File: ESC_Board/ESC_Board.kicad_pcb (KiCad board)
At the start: 4 copper layers, 73.2 x 50.8 mm, 199 parts, among them J1 63824-1, J2 63824-1, J3 63824-1, Q1 AO3400A, Q10 SIR182DP, Q11 SIR182Dp, Q12 SIR182DP, Q13 SIR182DP, Q14 SIR182DP, Q15 AO3400A, Q16 SIR182DP, Q17 SIR182DP, Q18 SIR182Dp, Q19 SIR182DP, Q2 AO3400A, Q20 SIR182DP, Q21 SIR182DP, Q22 AO3400A, Q23 SIR182DP, Q24 SIR182DP, Q25 SIR182Dp, Q26 SIR182DP, Q27 SIR182DP, Q28 SIR182DP, Q3 SIR182DP, Q4 SIR182DP, Q5 SIR182DP, Q6 SIR182Dp, Q7 SIR182DP, Q8 SIR182DP, Q9 SIR182DP, U10 DRV8300DRGER, U11 STM32F051K8Ux, U12 INA180A1, U13 DRV8300DRGER, U14 STM32F051K8Ux, U15 INA180A1, U2 STM32F051K8Ux, U3 INA180A1, U4 TPS62153RGTT, U5 DRV8300DRGER, U6 TLV76601QWDRBRQ1, U7 STM32F051K8Ux, U8 DRV8300DRGER, U9 INA180A1

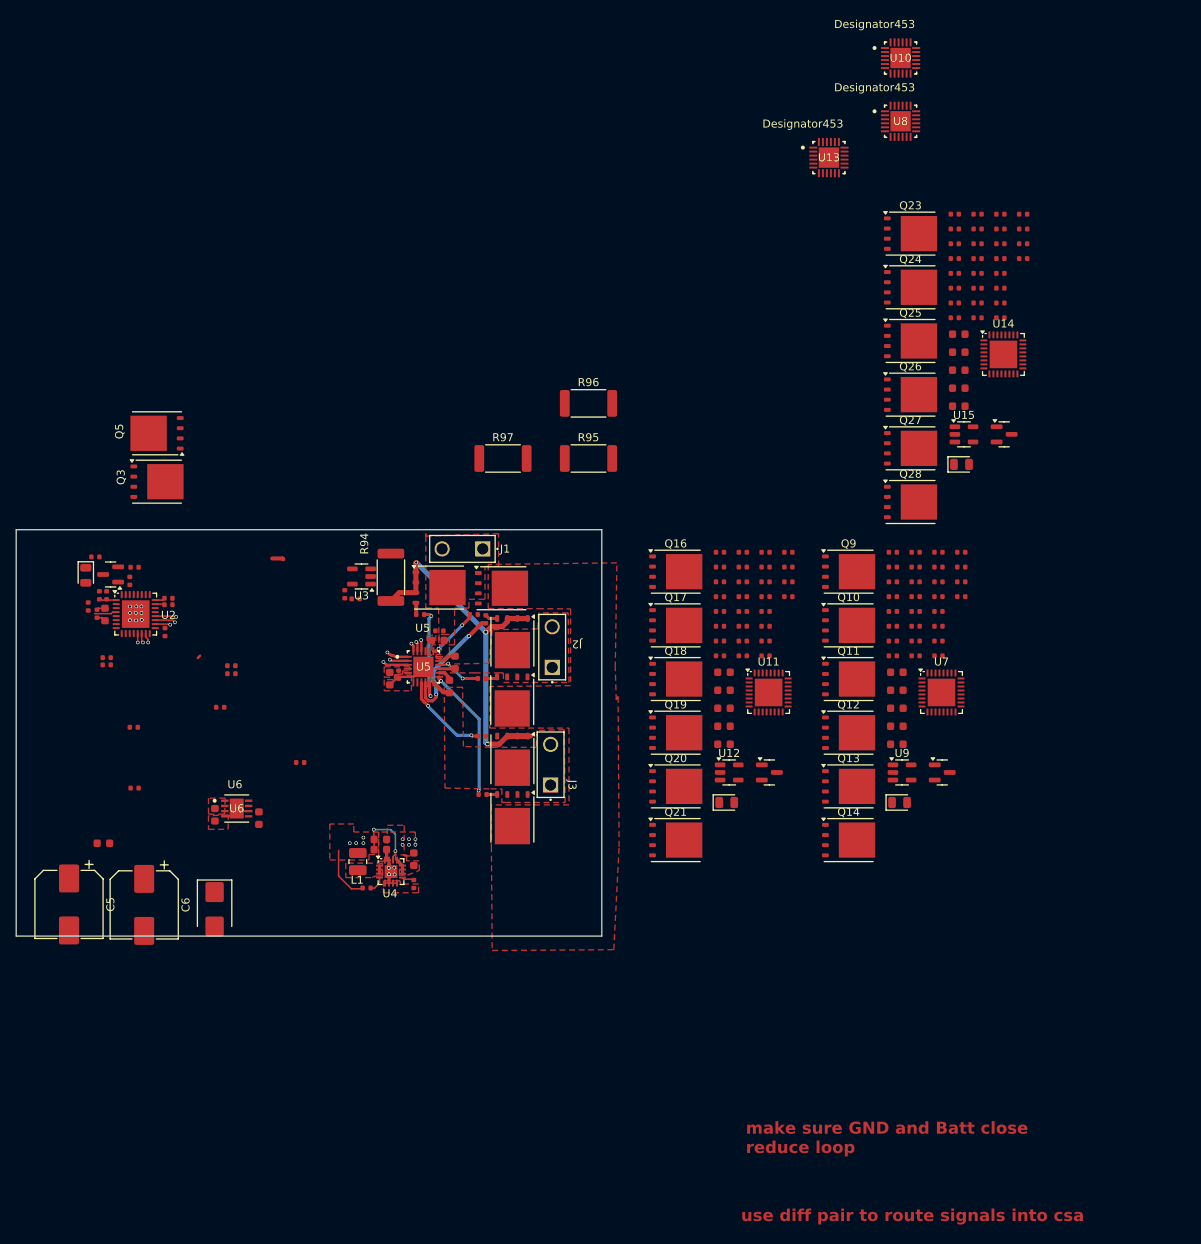
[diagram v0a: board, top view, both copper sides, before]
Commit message: ESC Board: Major overhauls to schematic, preliminary layout
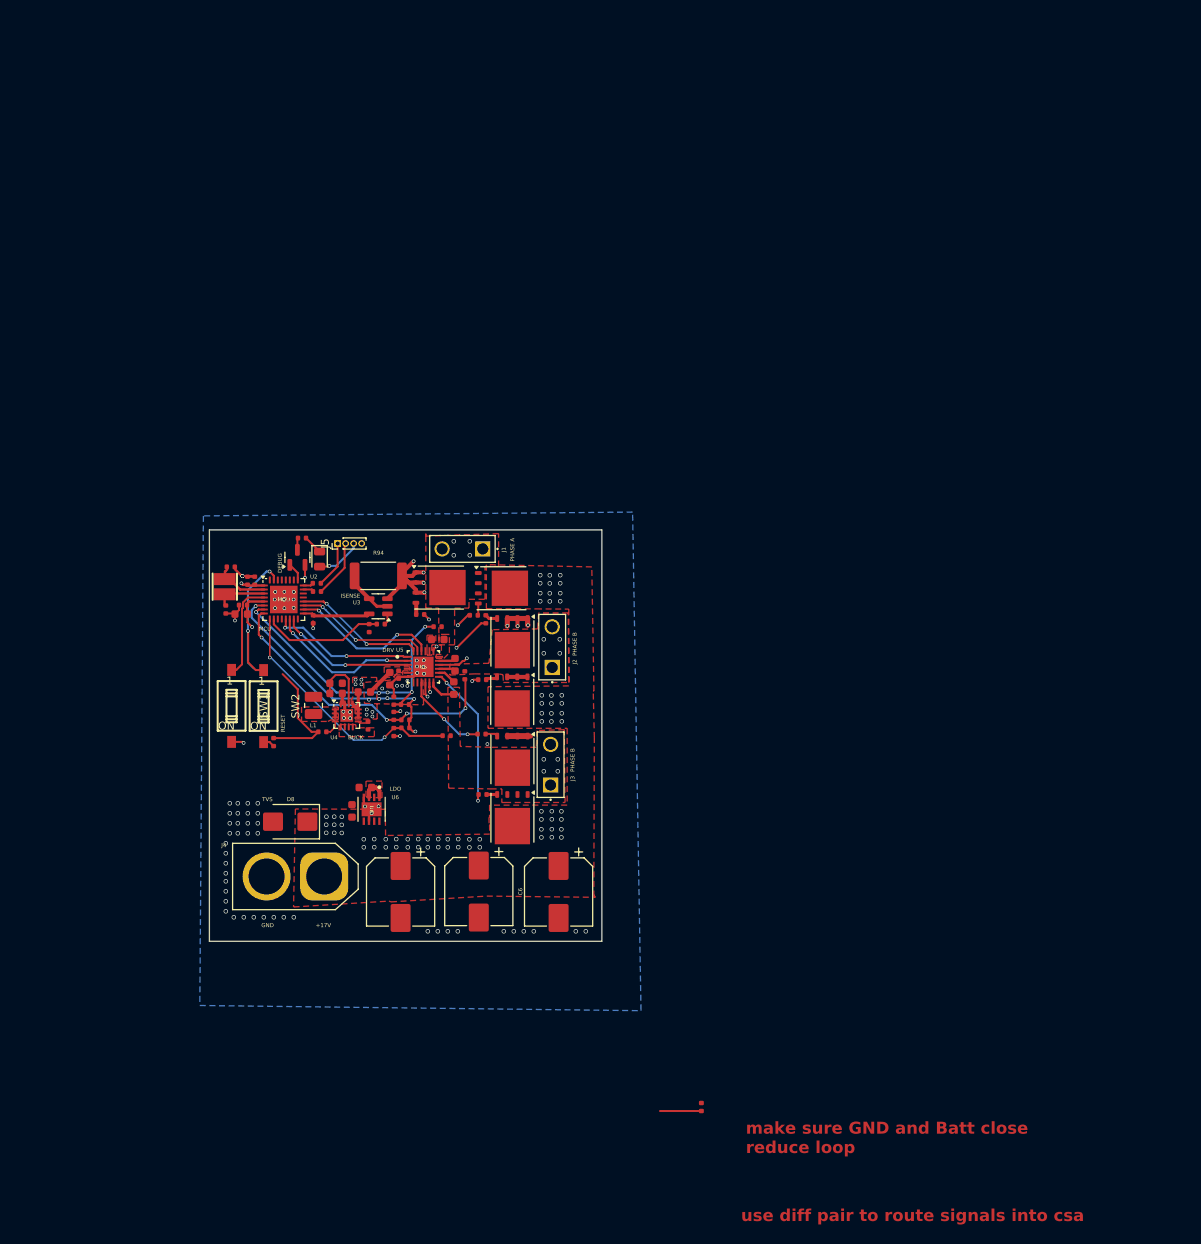
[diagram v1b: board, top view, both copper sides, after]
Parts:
- removed C14, C17, C2, C22, C3, C32, C34, C35, C4, C42, C44, C45: 100nF, PCM_JLCPCB:C_0402
- removed C18, C36, C46: 4.7uF, PCM_JLCPCB:C_0402
- removed C19, C40, C50: 10nF, PCM_JLCPCB:C_0402
- removed C27, C29, C30, C31, C37, C38, C39, C41, C47, C48, C49, C51: 1uF, PCM_JLCPCB:C_0603
- removed C28, C33, C43: 10uF, PCM_JLCPCB:C_0603
- removed D2, D4, D5: Red, PCM_JLCPCB:D_0805
- removed Q10, Q12, Q13, Q14, Q16, Q17, Q19, Q20, Q21, Q23, Q24, Q26, Q27, Q28, Q9: SIR182DP, Package_TO_SOT_SMD:TDSON-8-1
- removed Q11, Q18, Q25: SIR182Dp, Package_TO_SOT_SMD:TDSON-8-1
- removed Q15, Q2, Q22: AO3400A, PCM_JLCPCB:Q_SOT-23
- removed the Q3 at (58.4, 86.3)
- removed the Q5 at (58.4, 80.2)
- removed R10, R12, R28, R29, R30, R35, R37, R40, R42, R43, R47, R48, R49, R50, R56, R58, R62, R64, R66, R70, R71, R72, R73, R79, R81, R85, R87, R89, R93: 10kΩ, PCM_JLCPCB:R_0402
- removed R31, R32, R33, R34, R38, R39, R45, R46, R52, R53, R54, R55, R60, R61, R68, R69, R75, R76, R78, R8, R83, R84, R9, R91, R92: 22Ω, PCM_JLCPCB:R_0402
- removed R36, R41, R44, R57, R6, R63, R65, R67, R80, R86, R88, R90: 1kΩ, PCM_JLCPCB:R_0402
- removed R4, R51, R74: 75Ω, PCM_JLCPCB:R_0402
- removed R95, R96, R97: 3.0m, Resistor_SMD:R_2512_6332Metric
- removed U10, U13, U8: DRV8300DRGER, DRV:RGE0024B-IPC_A
- removed U11, U14, U7: STM32F051K8Ux, Package_DFN_QFN:QFN-32-1EP_5x5mm_P0.5mm_EP3.45x3.45mm
- removed U12, U15, U9: INA180A1, Package_TO_SOT_SMD:SOT-23-5
- added C55: 22pF, PCM_JLCPCB:C_0402, F.Cu at (67.6, 97.0)
- added C8: 100uF, Capacitor_SMD:CP_Elec_8x10, F.Cu at (108.6, 137.6)
- added J4: Conn_01x02_Pin, Connector_AMASS:AMASS_XT60-F_1x02_P7.20mm_Vertical, F.Cu at (79.3, 135.7)
- added J5: Conn_01x04_Pin, Connector_PinHeader_1.00mm:PinHeader_1x04_P1.00mm_Vertical, F.Cu at (81.0, 94.0)
- added R1: 100Ω, PCM_JLCPCB:R_0402, F.Cu at (78.4, 100.0)
- added R5: 100Ω, PCM_JLCPCB:R_0402, F.Cu at (78.4, 99.0)
- added SW1: SW_SPST, easy:SW-SMD_2P-L3.5-W6.2-P2.54-LS9.8, F.Cu at (67.7, 114.3)
- added SW2: SW_SPST, easy:SW-SMD_2P-L3.5-W6.2-P2.54-LS9.8, F.Cu at (71.7, 114.3)
- added Y1: Crystal_Small, easy:OSC-SMD_2P-L3.2-W2.5, F.Cu at (66.9, 99.4)
- C52: value 1uF -> 22pF; footprint PCM_JLCPCB:C_0603 -> PCM_JLCPCB:C_0402
- moved R77 109.8 mm to (126.5, 164.5), turned to 90 degrees
- moved C6 41.9 mm to (98.6, 137.5)
- moved C5 41.5 mm to (88.9, 137.6)
- moved R27 39.5 mm to (94.6, 118.0)
- moved R22 38.1 mm to (89.5, 116.1), turned to 180 degrees
- moved R23 36.4 mm to (88.0, 115.6), turned to 90 degrees
- moved C52 33.0 mm to (67.0, 102.3), turned to -90 degrees
- moved R26 32.5 mm to (88.0, 117.6), turned to -90 degrees
- moved D1 29.3 mm to (78.7, 96.0)
- moved R11 27.9 mm to (73.0, 118.8), turned to -90 degrees
- moved R3 25.9 mm to (76.5, 93.3), turned to 0 degrees
- moved Q1 23.4 mm to (76.0, 95.8), turned to 90 degrees
- moved R25 23.3 mm to (89.5, 117.1), turned to 180 degrees
- moved R24 23.3 mm to (96.9, 110.5), turned to 90 degrees
- moved R14 22.0 mm to (89.4, 114.2), turned to 180 degrees
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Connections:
- C52 pad 1: +17V -> Net-(U2-PF1)
- D8 pad 2: -LiPo -> GND
- R11 pad 1: GND -> +3.3V
- U2 pad 2: unconnected-(U2-PF0-Pad2) -> Net-(U2-PF0)
- U2 pad 25: unconnected-(U2-PA15-Pad25) -> Net-(Q1-G)
- U2 pad 3: unconnected-(U2-PF1-Pad3) -> Net-(U2-PF1)
- U2 pad 32: Net-(Q1-G) -> unconnected-(U2-PB8-Pad32)
- U2 pad 4: /SWDR -> Net-(SW1-A)
- U4 pad 6: AGND -> GND
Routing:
- net /BEMFB: track 0.00 -> 37.8 mm, vias 0 -> 4
- net /BEMFA: track 0.00 -> 37.8 mm, vias 0 -> 3
- net /BEMFCOMMON: track 0.00 -> 32.5 mm, vias 0 -> 3
- net /BEMFC: track 0.00 -> 31.5 mm, vias 0 -> 2
- net +3.3V: track 18.8 -> 45.4 mm, vias 6 -> 3
- net /LOW_COMMON: track 48.3 -> 26.7 mm, vias 4 -> 8
- net Net-(SW2-A): track 0.00 -> 21.3 mm, vias 0 -> 2
- net GND: track 16.3 -> 32.7 mm, vias 19 -> 81
- net /INHA: track 3.32 -> 18.8 mm
- net /INLB: track 3.49 -> 19.0 mm
- net /I_SENSE: track 0.00 -> 15.2 mm
- net /INLA: track 3.90 -> 18.0 mm
- net /INHB: track 3.79 -> 16.9 mm
- net /INHC: track 3.72 -> 16.6 mm
- net /INLC: track 4.44 -> 17.2 mm
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- added copper zone on In2.Cu, net +12V
- added copper zone on In2.Cu, net +3.3V
- added copper zone on In2.Cu, net /LOW_COMMON
- added copper zone on In2.Cu, net /MOTORB
- added copper zone on In2.Cu, net /MOTORC
- added copper zone on B.Cu, net GND
- added copper zone on In1.Cu, net GND
- removed copper zone on F.Cu, net +3.3V
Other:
- board size 73.2 x 50.8 mm -> 49 x 51.4 mm
- board text added: "+17V"
- board text added: "BUCK"
- board text added: "DEBUG"
- board text added: "DRV"
- board text added: "GND"
- board text added: "ISENSE"
- board text added: "LDO"
- board text added: "MCU"
- board text added: "PHASE A"
- board text added: "PHASE B"
- board text added: "RESET"
- board text added: "TVS"

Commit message: Finalized Layout for ESC Board
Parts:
- removed R77: 22Ω, PCM_JLCPCB:R_0402
- added G***: LOGO, LOGO, F.Cu at (104.8, 93.8)
- added J6: Conn_01x02_Pin, Connector_JST:JST_EH_B2B-EH-A_1x02_P2.50mm_Vertical, F.Cu at (71.0, 95.0)
- added REF**: MountingHole_2.1mm, MountingHole:MountingHole_2.1mm, F.Cu at (66.0, 142.6)
- added REF**: MountingHole_2.1mm, MountingHole:MountingHole_2.1mm, F.Cu at (110.0, 94.2)
- moved C12 1.65 mm to (68.8, 103.3), turned to -90 degrees
- moved C5 0.92 mm to (88.0, 137.8)
- moved C8 0.92 mm to (107.7, 137.8)
- moved C6 0.92 mm to (97.7, 137.7)
- moved C26 0.88 mm to (69.8, 102.8), turned to -90 degrees
- moved C55 0.85 mm to (67.1, 97.6)
- moved Y1 0.55 mm to (66.9, 100.0)
- moved J4 0.52 mm to (78.8, 135.8)
- moved C52 0.40 mm to (66.6, 102.3), turned to 0 degrees
- moved D8 0.23 mm to (75.2, 128.6)
- moved R24 0.18 mm to (96.8, 110.7)
- moved C10 0.06 mm to (77.9, 103.4)
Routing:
- net GND: track 32.7 -> 40.1 mm, vias 81 -> 107
- net Net-(SW2-A): track 21.3 -> 15.8 mm
- net /ESC4.sch2/GHA: track 5.18 -> 0.00 mm
- net +3.3V: track 45.4 -> 40.4 mm, vias 3 -> 9
- net /LOW_COMMON: track 26.7 -> 29.9 mm, vias 8 -> 15
- net +12V: track 10.7 -> 8.51 mm, vias 8 -> 20
- net Net-(U2-PF1): track 6.39 -> 7.95 mm
- net /GHB: track 7.76 -> 6.79 mm
- net +17V: vias 69 -> 59
- added copper zone on F.Cu, net +3.3V
- added copper zone on F.Cu, net /LOW_COMMON
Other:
- board size 49 x 51.4 mm -> 48.8 x 53.1 mm
- board text added: "+"
- board text added: "-"
- board text added: "BOOT"
- board text added: "CLK"
- board text added: "hot surface"
- board text removed: "DEBUG"

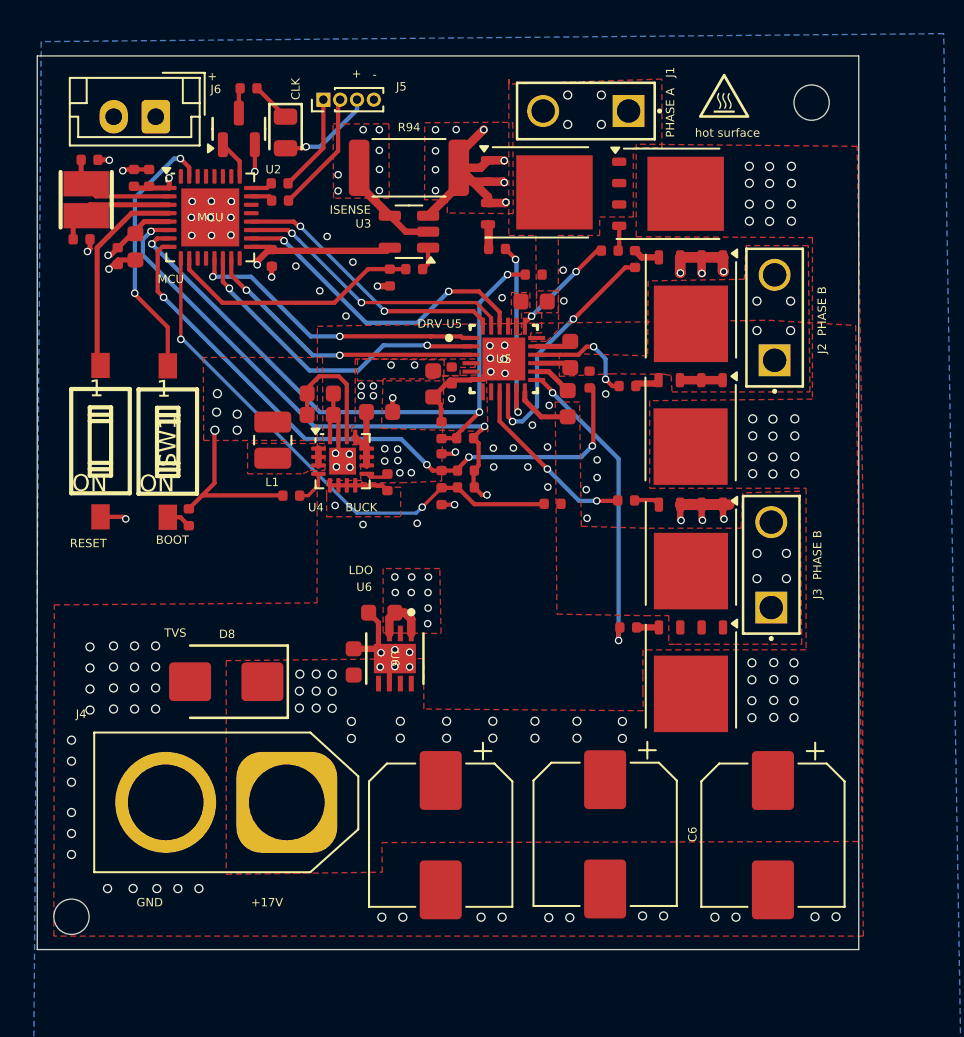
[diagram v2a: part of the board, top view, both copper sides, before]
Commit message: Optimized Signal Integrity, added stichting vias, and stiching capacitors between PWR and GND layers
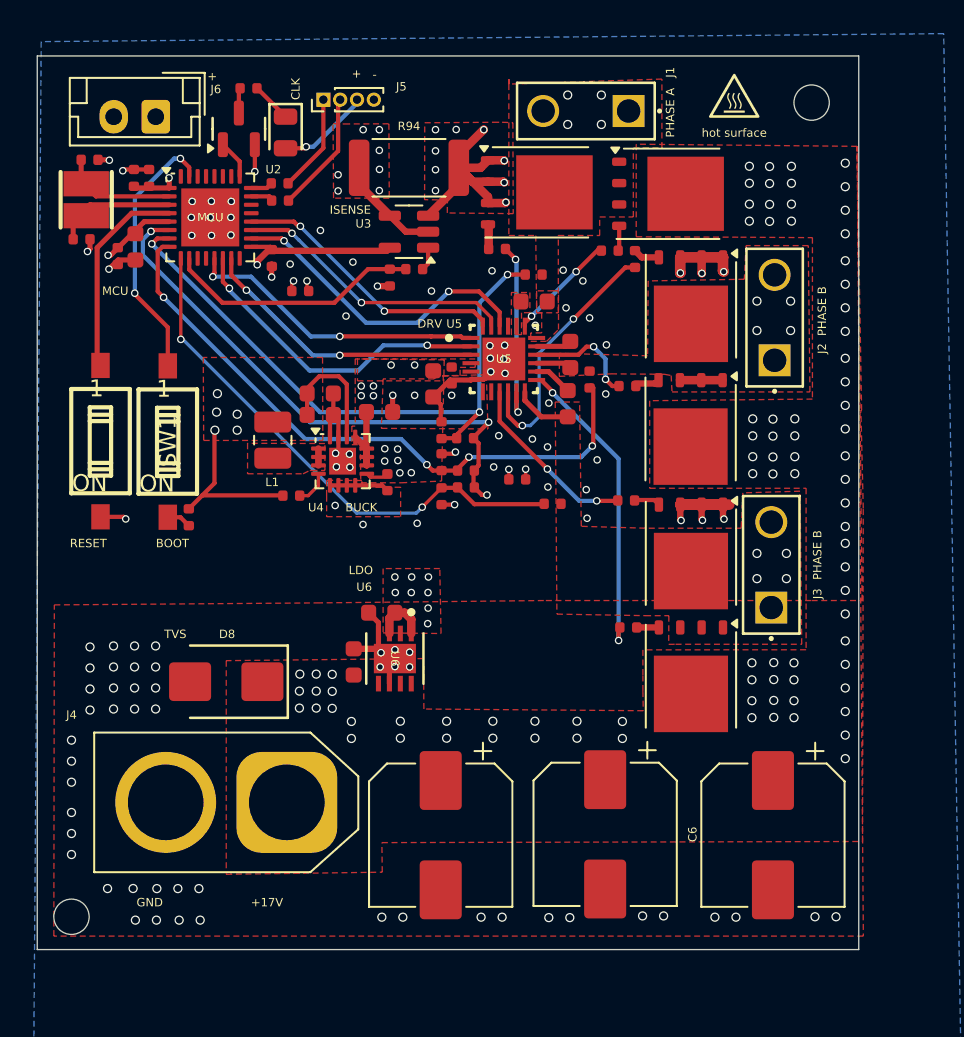
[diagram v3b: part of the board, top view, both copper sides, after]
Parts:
- added C56: 100nF, PCM_JLCPCB:C_0402, F.Cu at (79.6, 105.4)
- added C58: 100nF, PCM_JLCPCB:C_0402, F.Cu at (92.5, 116.6)
- moved G*** 0.60 mm to (105.4, 93.8)
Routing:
- net GND: track 40.1 -> 41.5 mm, vias 107 -> 141
- net +12V: track 8.51 -> 9.11 mm, vias 20 -> 21
- net /GLB: track 14.7 -> 15.3 mm
- net +3.3V: track 40.4 -> 40.8 mm, vias 9 -> 10
